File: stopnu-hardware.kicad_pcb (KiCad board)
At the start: 4 copper layers, 94 x 131 mm, 56 parts, among them CN1 SM04B-SRSS-TB (LF)(SN), CN3 OQ0232510000G, CN4 OQ0232510000G, CN5 OQ0232510000G, CN6 OQ0432510000G, J1 Conn_02x15_Odd_Even, U1 WIFI_KIT_32__V3_, U19 SY6280AAC, U2 74HCT1G125GW-Q100H, U3 LD1117V33, U5 LTV-817S, U6 LTV-817S, U7 LTV-817S

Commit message: WIP: Routed version, for first feedback round
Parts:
- added CN2: OQ0232510000G, lcsc:CONN-TH_OQ0232510000G, F.Cu at (4.03, 70.1)
- added D1: D5V0P4URL6SO-7, lcsc:SOT-26_L3.0-W1.6-P0.95-LS2.8-BL, F.Cu at (-7.73, 65.5)
- added D2: ESD prot., Diode_SMD:D_SOD-323, F.Cu at (3.37, 65.5)
- added N1: Viking Art, footprints:StopNuVikings, F.Cu at (-1.08, -36.0)
- added R1: 2k, Resistor_SMD:R_0603_1608Metric, F.Cu at (-9.23, 61.5)
- added R2: 2k, Resistor_SMD:R_0603_1608Metric, F.Cu at (-6.23, 61.5)
- added TP3: TestPoint, TestPoint:TestPoint_Pad_D1.0mm, F.Cu at (6.32, 61.8)
- added U4: 74HCT1G125GW-Q100H, lcsc:TSSOP-5_L2.1-W1.3-P0.65-LS2.2-BL, F.Cu at (3.06, 62.0)
- TP1: value TestPoint -> MCU_TX
- TP2: value TestPoint -> MCU_RX
- moved U3 65.5 mm to (-42.0, 70.0), turned to 90 degrees
- moved C15 61.7 mm to (-38.2, 71.2)
- moved JP2 56.4 mm to (-42.6, 61.2)
- moved C16 54.6 mm to (-38.5, 67.0)
- moved TP5 45.2 mm to (17.0, 61.6)
- moved D4 39.2 mm to (13.9, 65.1), turned to 180 degrees
- moved CN4 36.1 mm to (15.0, 70.1)
- moved U2 33.4 mm to (13.9, 61.8), turned to -90 degrees
- moved R3 22.0 mm to (-25.8, 62.9)
- moved C5 21.9 mm to (-21.9, 59.3)
- moved C6 21.9 mm to (-21.9, 62.9)
- moved CN3 19.0 mm to (-20.0, 70.1)
- moved TP2 16.8 mm to (-28.8, 53.0)
- moved CN6 15.7 mm to (31.2, 70.1)
- moved TP8 14.2 mm to (26.0, 61.0)
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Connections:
- net /LED control output/DOUT renamed /LED control output 1/DOUT
- C5 pad 1: /Ambient light sensor/V_AMLIGHT_EM -> /GPIO02
- C6 pad 1: /Ambient light sensor/V_AMLIGHT_EM -> /GPIO02
- CN3 pad 1: /Ambient light sensor/V_AMLIGHT_EM -> /GPIO02
- J1 pad 15: +5V -> +3V3
- J1 pad 16: +3V3 -> +5V
- JP1 pad 2: +3V3 -> +3V3_MCU
- R3 pad 1: /Ambient light sensor/V_AMLIGHT_EM -> /GPIO02
- R5 pad 2: /GPIO5 -> /GPIO07
- R7 pad 2: /GPIO6 -> /GPIO06
- R9 pad 2: /GPIO7 -> /GPIO05
- TP10 pad 1: /GPIO6 -> /GPIO06
- TP11 pad 1: /GPIO7 -> /GPIO05
- TP12 pad 1: /GPIO5 -> /GPIO07
- U1 pad J3_2: +3V3 -> +3V3_MCU
- U1 pad J3_3: +3V3 -> +3V3_MCU
- U2 pad 2: /LED control output/DIN -> /GPIO04
- U5 pad 4: /GPIO6 -> /GPIO06
- U6 pad 4: /GPIO7 -> /GPIO05
- U7 pad 4: /GPIO5 -> /GPIO07
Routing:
- net +5V: track 0.00 -> 210.5 mm, vias 0 -> 4
- net /GPIO47: track 0.00 -> 70.4 mm
- net /GPIO02: track 0.00 -> 70.0 mm
- net /GPIO48: track 0.00 -> 69.6 mm
- net /GPIO04: track 0.00 -> 63.8 mm
- net /GPIO03: track 0.00 -> 60.8 mm
- net /GPIO07: track 0.00 -> 59.7 mm
- net /GPIO06: track 0.00 -> 53.2 mm, vias 0 -> 1
- net /GPIO05: track 0.00 -> 49.6 mm, vias 0 -> 1
- net /UART_RX: track 0.00 -> 49.5 mm
- net /UART_TX: track 0.00 -> 48.9 mm
- net /MCU_RST: track 0.00 -> 45.1 mm
- net /USER_KEY: track 0.00 -> 45.1 mm
- net /GPIO26: track 0.00 -> 45.1 mm
- net /GPIO33: track 0.00 -> 43.0 mm
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
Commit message: WIP: Added StopNu temp text label.
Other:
- board text added: "STOPNU"

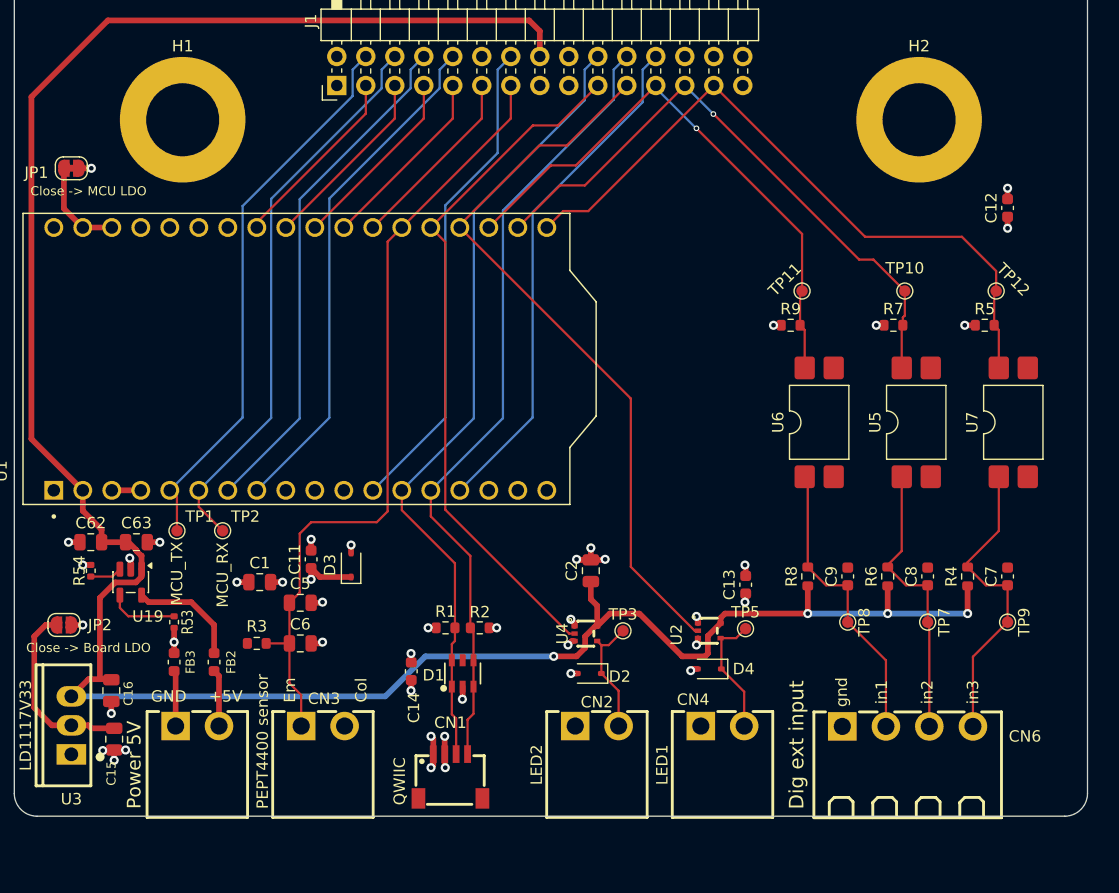
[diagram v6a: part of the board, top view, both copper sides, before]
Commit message: Add some vias around GND, STOPNU label
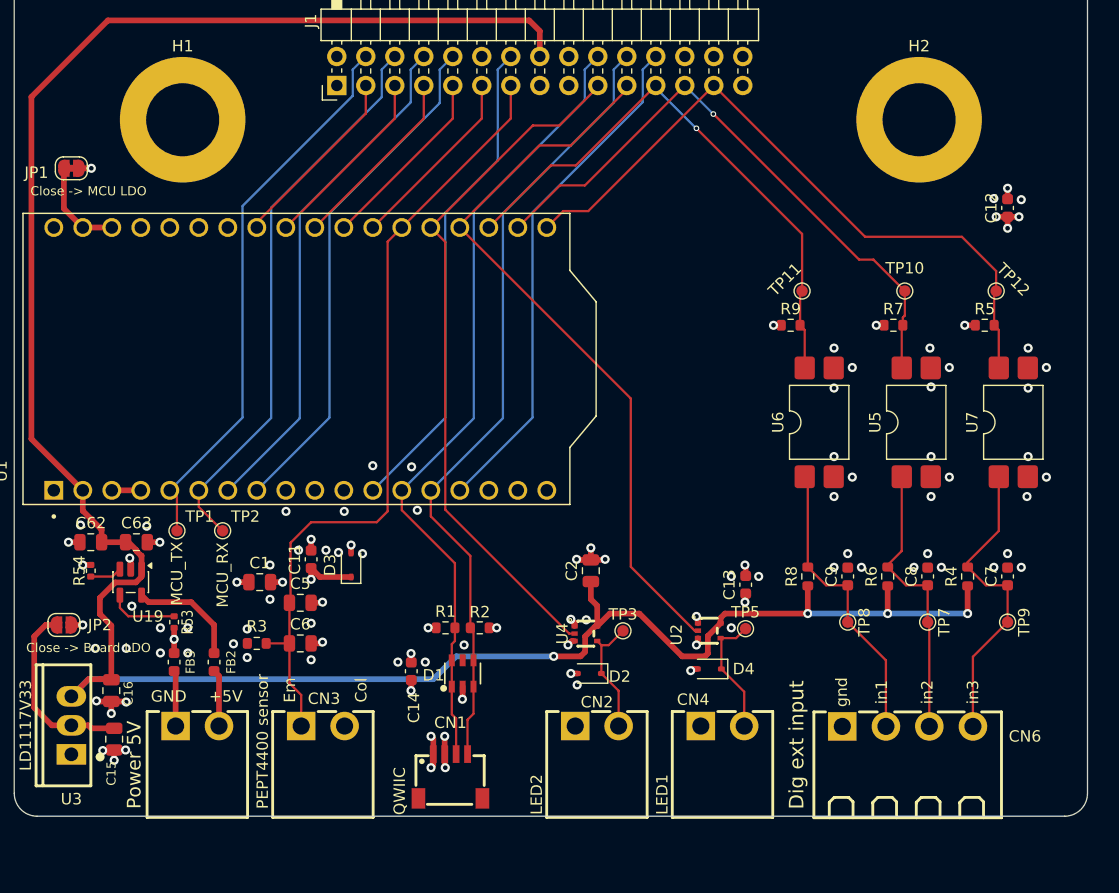
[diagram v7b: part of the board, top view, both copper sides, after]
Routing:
- net GND: track 29.1 -> 31.7 mm, vias 29 -> 93
- net +3V3: track 17.0 -> 19.0 mm, vias 14 -> 16
- net +5V: track 210.5 -> 211.2 mm

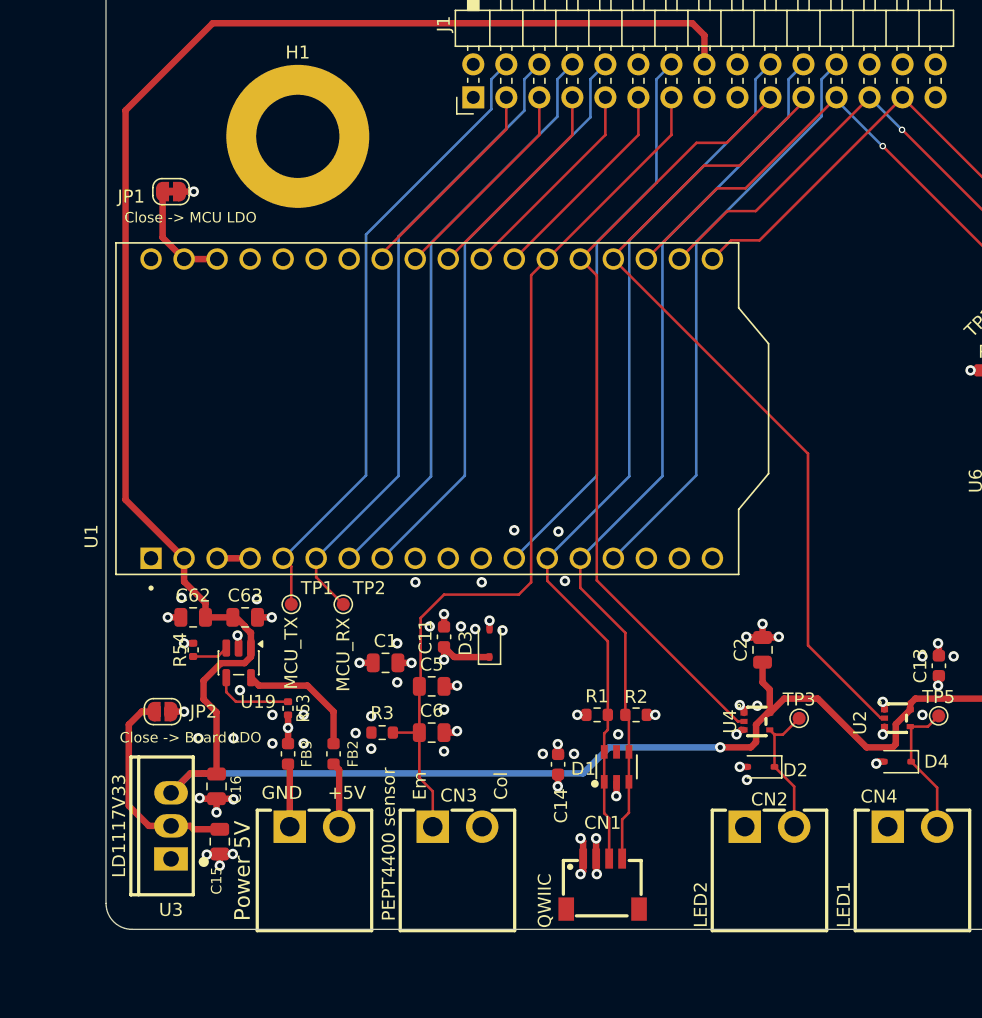
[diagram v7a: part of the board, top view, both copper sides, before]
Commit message: moved heltec V3 4mm down
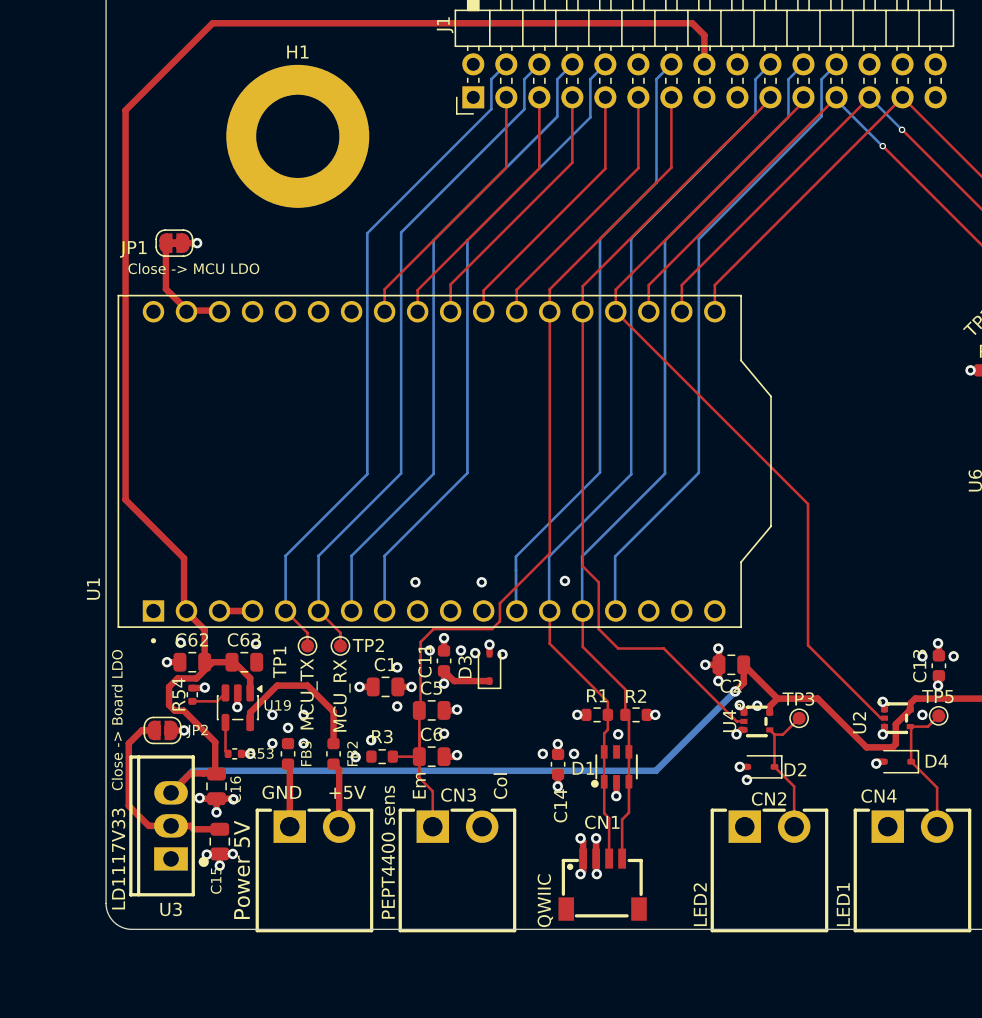
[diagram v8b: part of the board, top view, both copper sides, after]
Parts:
- moved R53 5.39 mm to (-37.1, 64.5), turned to 0 degrees
- moved U1 4.06 mm to (-20.9, 42.0)
- moved JP1 3.97 mm to (-41.7, 25.2)
- moved C62 3.45 mm to (-40.4, 57.5)
- moved C63 3.45 mm to (-36.4, 57.5)
- moved R54 3.45 mm to (-40.4, 60.0)
- moved U19 3.45 mm to (-36.9, 61.0)
- moved TP1 3.44 mm to (-31.5, 56.2)
- moved TP2 3.21 mm to (-29.0, 56.2)
- moved C2 2.66 mm to (1.10, 57.6), turned to 180 degrees
- moved C1 1.85 mm to (-25.5, 59.4)
- moved C11 1.85 mm to (-21.0, 57.4)
- moved C5 1.85 mm to (-21.9, 61.2)
- moved C6 1.85 mm to (-21.9, 64.7)
- moved D3 1.85 mm to (-17.5, 57.9)
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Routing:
- net /GPIO41: track 16.0 -> 20.4 mm
- net /GPIO33: track 43.0 -> 47.0 mm
- net /GPIO26: track 45.1 -> 49.1 mm
- net /MCU_RST: track 45.1 -> 49.1 mm
- net /GPIO40: track 16.4 -> 20.4 mm
- net /GPIO38: track 16.4 -> 20.4 mm
- net /GPIO01: track 16.4 -> 20.4 mm
- net /GPIO39: track 16.4 -> 20.4 mm
- net /USER_KEY: track 45.1 -> 49.1 mm
- net Net-(U19-ON): track 6.17 -> 2.50 mm
- net /UART_TX: track 48.9 -> 52.5 mm
- net /UART_RX: track 49.5 -> 52.5 mm
- net /GPIO06: track 53.2 -> 55.9 mm
- net /GPIO07: track 59.7 -> 62.4 mm
- net /GPIO05: track 49.6 -> 52.3 mm
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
